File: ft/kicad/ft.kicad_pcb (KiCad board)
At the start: 2 copper layers, 28 x 38.5 mm, 2 parts, among them J1 Conn_RIOT, J2 Conn_ft

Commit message: Update logo
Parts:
- added G***: LOGO, LOGO, F.Cu at (101.3, 57.4)
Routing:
- net /LOAD_OUT: track 25.9 -> 26.6 mm
- net /TRIGGER_Y: track 14.9 -> 14.3 mm
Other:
- board text added: "CI Adapter"
- board text removed: "TOP"
- board text removed: "ftPAL"

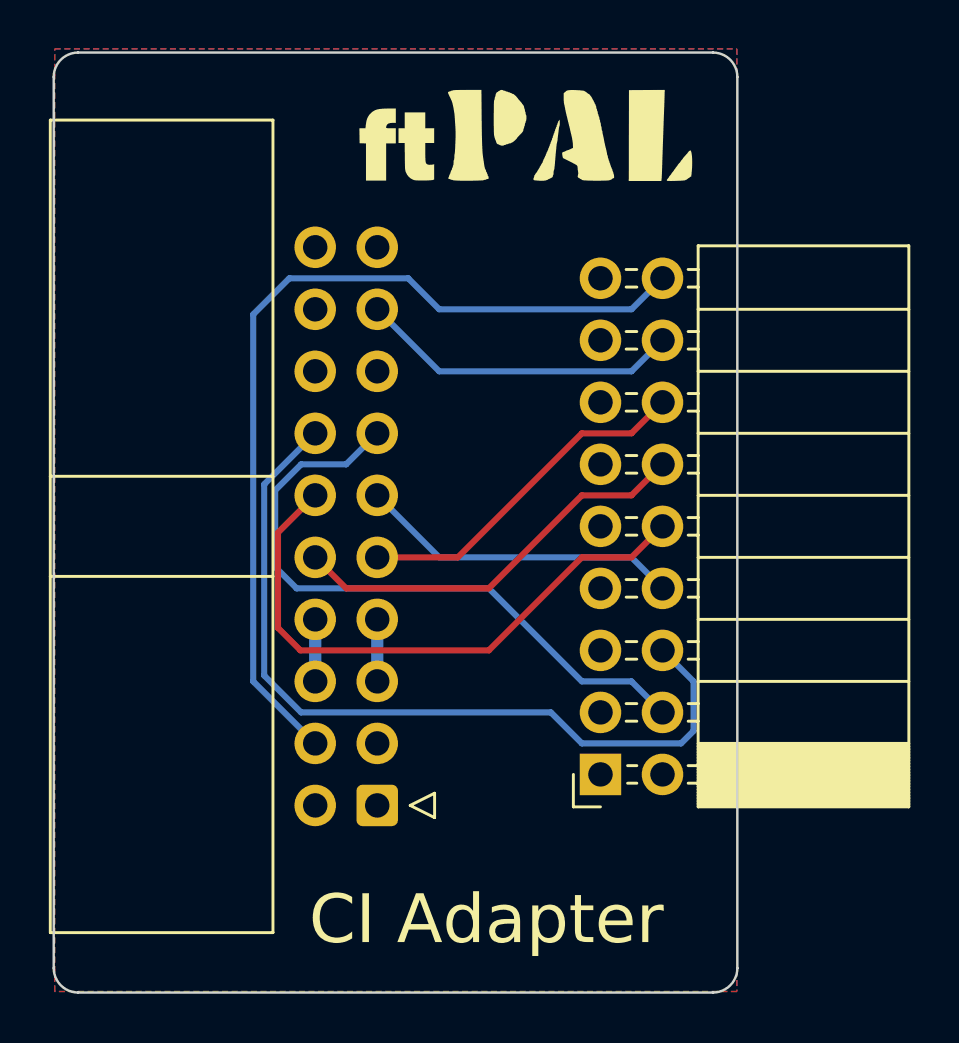
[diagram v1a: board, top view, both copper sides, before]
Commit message: Add DATA_IN selection jumper
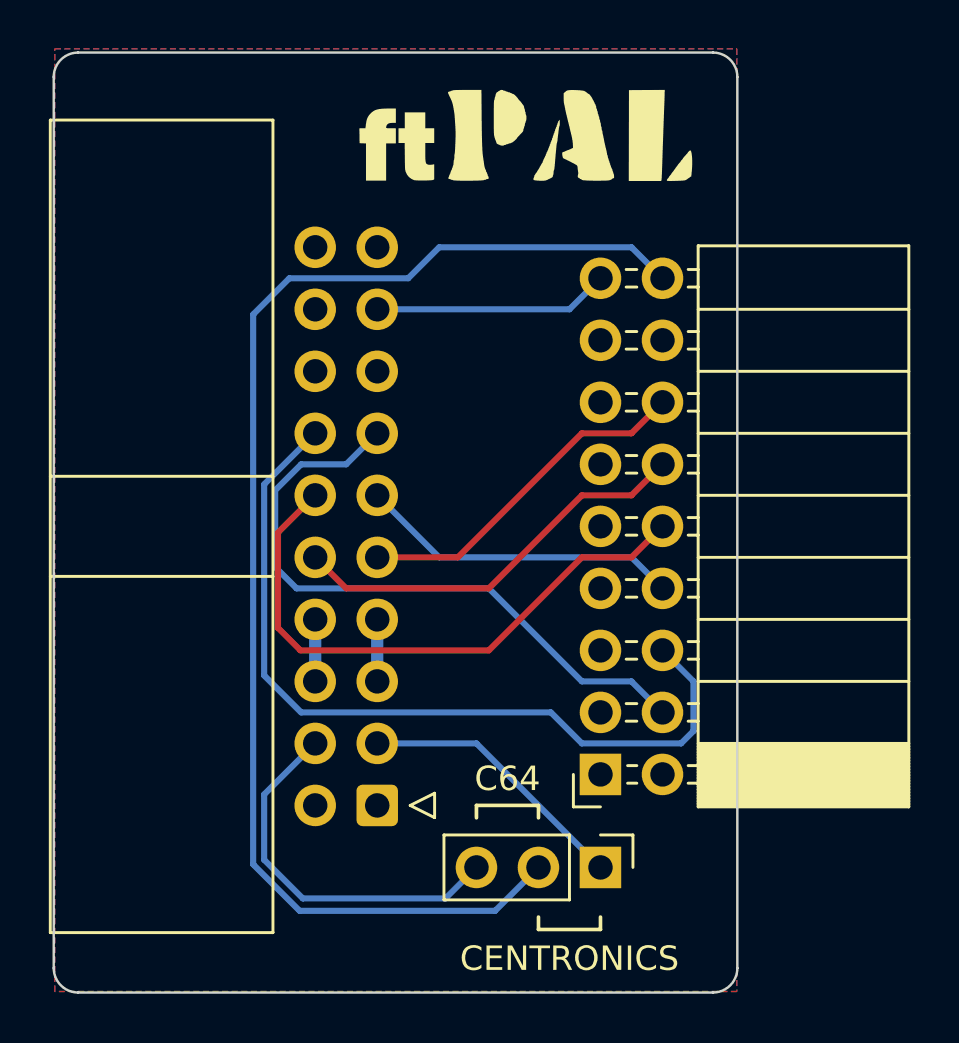
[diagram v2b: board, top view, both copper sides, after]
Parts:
- added JP1: Input_Select, Connector_PinHeader_2.54mm:PinHeader_1x03_P2.54mm_Vertical, F.Cu at (104.4, 87.4)
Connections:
- J1 pad 16: /COUNT_IN -> unconnected-(J1-Pin_16-Pad16)
- J1 pad 17: unconnected-(J1-Pin_17-Pad17) -> /COUNT_IN
- J2 pad 3: unconnected-(J2-Pin_3-Pad3) -> /CENTRONICS_DATA_IN
- J2 pad 4: /DATA_IN -> /C64_DATA_IN
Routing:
- net /DATA_IN: track 37.1 -> 54.2 mm
- net /C64_DATA_IN: track 0.00 -> 15.5 mm
- net /CENTRONICS_DATA_IN: track 0.00 -> 11.2 mm
- net /COUNT_IN: track 13.3 -> 9.67 mm
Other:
- board text added: "C64"
- board text added: "CENTRONICS"
- board text removed: "CI Adapter"
